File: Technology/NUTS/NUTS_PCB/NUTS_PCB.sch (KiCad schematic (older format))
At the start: 47 parts, among them J1 Micro_SD_Card_Det_Hirose_DM3AT, J2 USB_B_Micro, J3 Jack-DC, J4 Conn_01x06_Female, J5 Conn_01x03_Male, J6 Conn_01x03_Female, J7 Conn_01x02_Female, J8 Conn_01x02_Male, J9 Screw_Terminal_01x02, Q1 DMG3415UFY4Q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

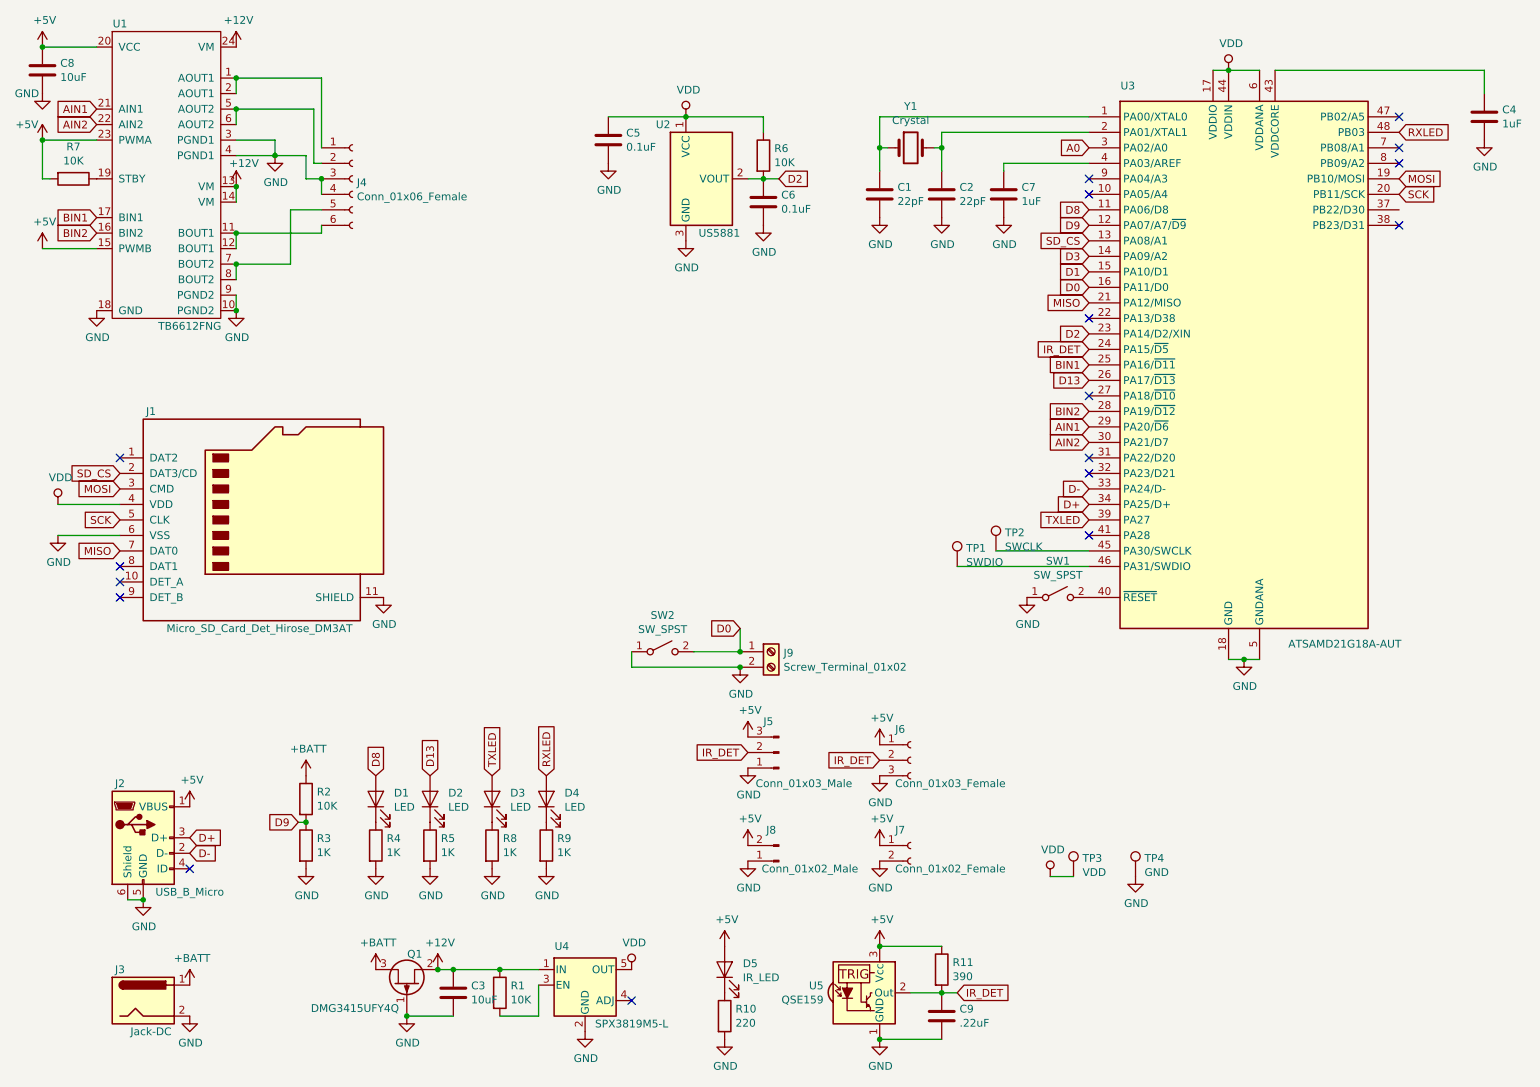
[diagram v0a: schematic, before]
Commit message: Got Nuts PCB prototype working, needs updates
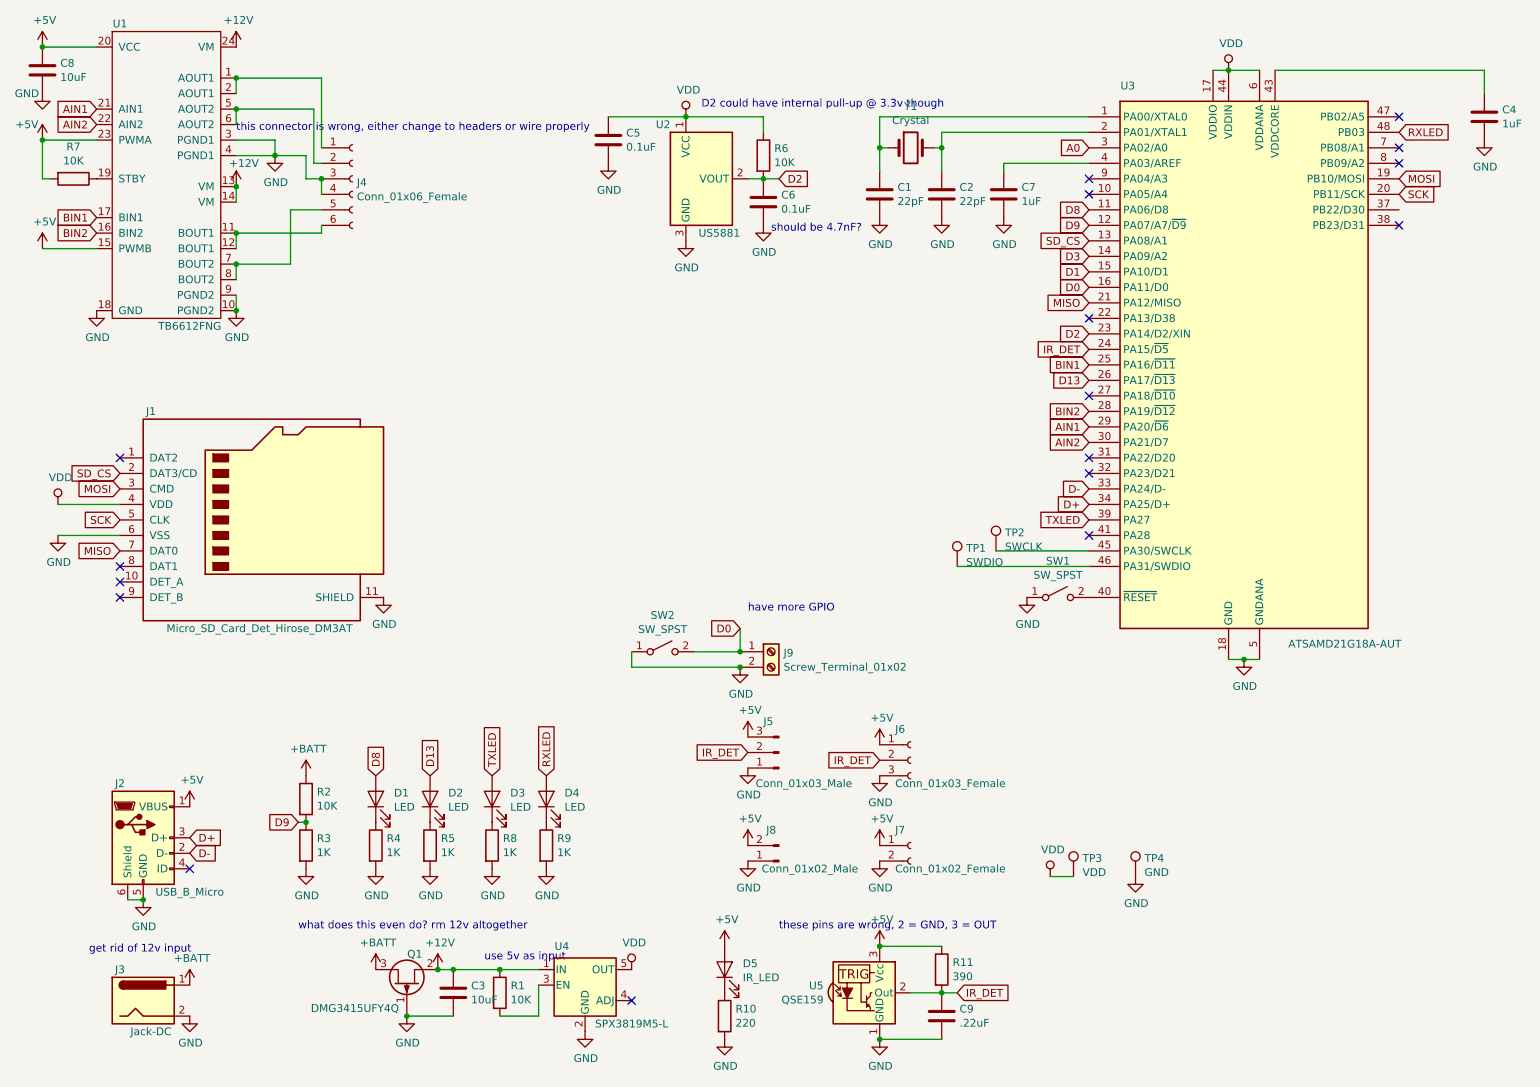
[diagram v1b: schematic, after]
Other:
- note added: "D2 could have internal pull-up @ 3.3v though"
- note added: "get rid of 12v input"
- note added: "have more GPIO"
- note added: "should be 4.7nF?"
- note added: "these pins are wrong, 2 = GND, 3 = OUT"
- note added: "this connector is wrong, either change to headers or wire properly"
- note added: "use 5v as input"
- note added: "what does this even do? rm 12v altogether"
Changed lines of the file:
@@
 	1    0    0    -1
 $EndComp
+Text Notes 4900 1250 0    50   ~ 0
+D2 could have internal pull-up @ 3.3v though
+Text Notes 2300 6550 0    50   ~ 0
+what does this even do? rm 12v altogether
+Text Notes 5350 2050 0    50   ~ 0
+should be 4.7nF?
+Text Notes 5400 6550 0    50   ~ 0
+these pins are wrong, 2 = GND, 3 = OUT
+Text Notes 3500 6750 0    50   ~ 0
+use 5v as input
+Text Notes 5200 4500 0    50   ~ 0
+have more GPIO
+Text Notes 1900 1400 0    50   ~ 0
+this connector is wrong, either change to headers or wire properly
+Text Notes 950  6700 0    50   ~ 0
+get rid of 12v input
 $EndSCHEMATC

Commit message: Working on pink noise
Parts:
- U3: symbol MCU_Microchip_SAMD:ATSAMD21G18A-AUT -> NUTS_PCB-rescue:ATSAMD21G18A-AUT-MCU_Microchip_SAMD
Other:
- note added: "Probably need input diode on 5V USB if used for motor!"
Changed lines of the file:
@@
 $EndComp
 $Comp
-L MCU_Microchip_SAMD:ATSAMD21G18A-AUT U3
+L NUTS_PCB-rescue:ATSAMD21G18A-AUT-MCU_Microchip_SAMD U3
 U 1 1 5E79844E
 P 8400 2900
@@
 Text Notes 950  6700 0    50   ~ 0
 get rid of 12v input
+Text Notes 1000 2950 0    50   ~ 0
+Probably need input diode on 5V USB if used for motor!
 $EndSCHEMATC
